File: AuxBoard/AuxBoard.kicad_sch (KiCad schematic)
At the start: 29 parts, among them J1 ATX-24, J10 MatBIn, J11 FanHeader, J2 RPI4B, J4 MatrixASupply, J5 MatrixBSupply, J6 BigLED, J7 MatAOut, J8 MatAIn, J9 MatBOut, Q1 DMMT5401, Q2 DMG2305UX, Q3 DMG2305UX, Q4 DMG2305UX, SW1 SW_DPST, U1 74AHC04

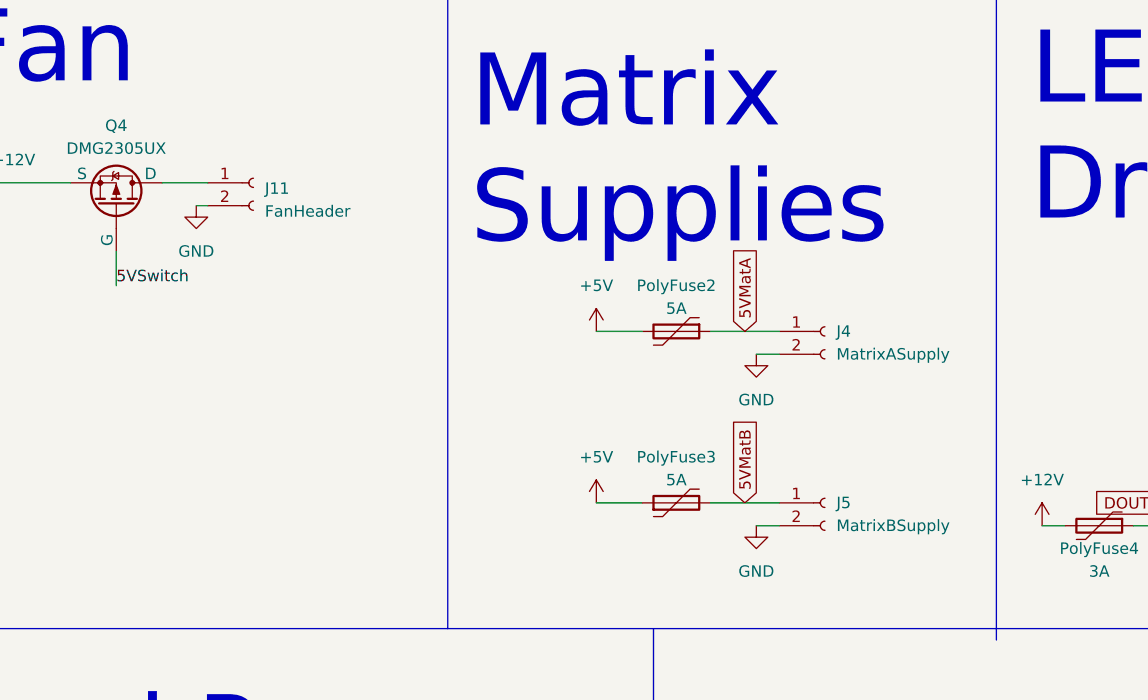
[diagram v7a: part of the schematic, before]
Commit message: Fixing Header Orientation
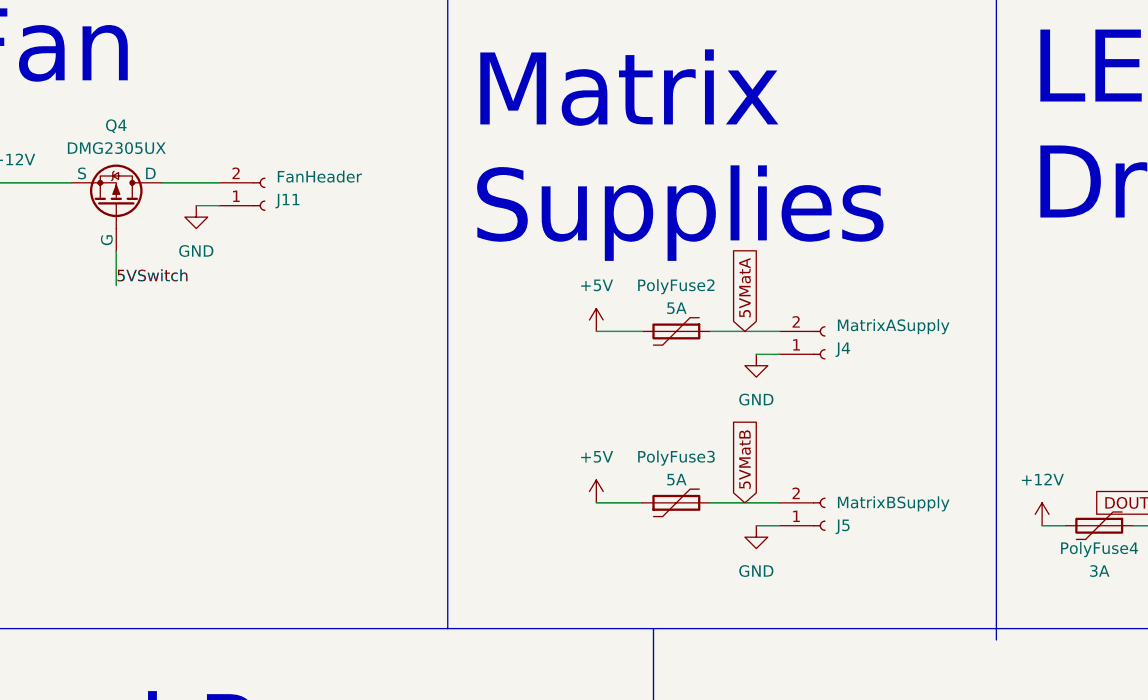
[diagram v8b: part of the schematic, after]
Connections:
- net 5VMatA: now also J4.2 (Pin_2); no longer J4.1 (Pin_1)
- net 5VMatB: now also J5.2 (Pin_2); no longer J5.1 (Pin_1)
- net GND: now also J11.1 (Pin_1), J4.1 (Pin_1), J5.1 (Pin_1); no longer J11.2 (Pin_2), J4.2 (Pin_2), J5.2 (Pin_2)
- net at Q4.1 (D): now also J11.2 (Pin_2); no longer J11.1 (Pin_1)
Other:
- moved on the sheet: J11
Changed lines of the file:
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@@
     (stroke (width 0) (type default))
   )
-  (wire (pts (xy 121.92 34.29) (xy 127 34.29))
+  (wire (pts (xy 190.5 69.85) (xy 182.88 69.85))
     (stroke (width 0) (type default))
   )
@@
     (stroke (width 0) (type default))
   )
+  (wire (pts (xy 121.92 34.29) (xy 128.27 34.29))
+    (stroke (width 0) (type default))
+  )
   (wire (pts (xy 140.97 109.22) (xy 135.89 109.22))
     (stroke (width 0) (type default))
@@
     (stroke (width 0) (type default))
   )
-  (wire (pts (xy 182.88 69.85) (xy 190.5 69.85))
-    (stroke (width 0) (type default))
-  )
   (wire (pts (xy 262.89 67.31) (xy 266.7 67.31))
     (stroke (width 0) (type default))
@@
     (stroke (width 0) (type default))
   )
-  (wire (pts (xy 125.73 36.83) (xy 127 36.83))
-    (stroke (width 0) (type default))
-  )
   (wire (pts (xy 34.29 139.7) (xy 39.37 139.7))
     (stroke (width 0) (type default))
@@
   )
   (wire (pts (xy 91.44 149.86) (xy 96.52 149.86))
+    (stroke (width 0) (type default))
+  )
+  (wire (pts (xy 125.73 36.83) (xy 128.27 36.83))
     (stroke (width 0) (type default))
   )
@@
     )
   )
-  (symbol (lib_id "Connector:Conn_01x02_Female") (at 195.58 69.85 0) (unit 1)
-    (in_bom yes) (on_board yes) (dnp no) (fields_autoplaced)
-    (property "Reference" "J5" (at 196.85 69.8499 0)
-      (effects (font (size 1.27 1.27)) (justify left))
-    )
-    (property "Value" "MatrixBSupply" (at 196.85 72.3899 0)
-      (effects (font (size 1.27 1.27)) (justify left))
-    )
-    (property "Footprint" "Connector_PinSocket_2.54mm:PinSocket_1x02_P2.54mm_Vertical" (at 195.58 69.85 0)
-      (effects (font (size 1.27 1.27)) hide)
-    )
-    (property "Datasheet" "~" (at 195.58 69.85 0)
+  (symbol (lib_id "Connector:Conn_01x02_Female") (at 195.58 72.39 0) (mirror x) (unit 1)
+    (in_bom yes) (on_board yes) (dnp no)
+    (property "Reference" "J5" (at 196.85 72.3901 0)
+      (effects (font (size 1.27 1.27)) (justify left))
+    )
+    (property "Value" "MatrixBSupply" (at 196.85 69.8501 0)
+      (effects (font (size 1.27 1.27)) (justify left))
+    )
+    (property "Footprint" "Connector_PinSocket_2.54mm:PinSocket_1x02_P2.54mm_Vertical" (at 195.58 72.39 0)
+      (effects (font (size 1.27 1.27)) hide)
+    )
+    (property "Datasheet" "~" (at 195.58 72.39 0)
       (effects (font (size 1.27 1.27)) hide)
     )
@@
     )
   )
-  (symbol (lib_id "Connector:Conn_01x02_Female") (at 195.58 50.8 0) (unit 1)
-    (in_bom yes) (on_board yes) (dnp no) (fields_autoplaced)
-    (property "Reference" "J4" (at 196.85 50.7999 0)
-      (effects (font (size 1.27 1.27)) (justify left))
-    )
-    (property "Value" "MatrixASupply" (at 196.85 53.3399 0)
-      (effects (font (size 1.27 1.27)) (justify left))
-    )
-    (property "Footprint" "Connector_PinSocket_2.54mm:PinSocket_1x02_P2.54mm_Vertical" (at 195.58 50.8 0)
-      (effects (font (size 1.27 1.27)) hide)
-    )
-    (property "Datasheet" "~" (at 195.58 50.8 0)
+  (symbol (lib_id "Connector:Conn_01x02_Female") (at 195.58 53.34 0) (mirror x) (unit 1)
+    (in_bom yes) (on_board yes) (dnp no)
+    (property "Reference" "J4" (at 196.85 52.705 0)
+      (effects (font (size 1.27 1.27)) (justify left))
+    )
+    (property "Value" "MatrixASupply" (at 196.85 50.165 0)
+      (effects (font (size 1.27 1.27)) (justify left))
+    )
+    (property "Footprint" "Connector_PinSocket_2.54mm:PinSocket_1x02_P2.54mm_Vertical" (at 195.58 53.34 0)
+      (effects (font (size 1.27 1.27)) hide)
+    )
+    (property "Datasheet" "~" (at 195.58 53.34 0)
       (effects (font (size 1.27 1.27)) hide)
     )
@@
     )
   )
-  (symbol (lib_id "Connector:Conn_01x02_Female") (at 132.08 34.29 0) (unit 1)
-    (in_bom yes) (on_board yes) (dnp no) (fields_autoplaced)
-    (property "Reference" "J11" (at 133.35 34.925 0)
-      (effects (font (size 1.27 1.27)) (justify left))
-    )
-    (property "Value" "FanHeader" (at 133.35 37.465 0)
-      (effects (font (size 1.27 1.27)) (justify left))
-    )
-    (property "Footprint" "Connector_PinSocket_2.54mm:PinSocket_1x02_P2.54mm_Vertical" (at 132.08 34.29 0)
-      (effects (font (size 1.27 1.27)) hide)
-    )
-    (property "Datasheet" "~" (at 132.08 34.29 0)
-      (effects (font (size 1.27 1.27)) hide)
-    )
+  (symbol (lib_id "Connector:Conn_01x02_Female") (at 133.35 36.83 0) (mirror x) (unit 1)
+    (in_bom yes) (on_board yes) (dnp no)
+    (property "Reference" "J11" (at 134.62 36.195 0)
+      (effects (font (size 1.27 1.27)) (justify left))
+    )
+    (property "Value" "FanHeader" (at 134.62 33.655 0)
+      (effects (font (size 1.27 1.27)) (justify left))
+    )
+    (property "Footprint" "Connector_PinSocket_2.54mm:PinSocket_1x02_P2.54mm_Vertical" (at 133.35 36.83 0)
+      (effects (font (size 1.27 1.27)) hide)
+    )
+    (property "Datasheet" "~" (at 133.35 36.83 0)
+      (effects (font (size 1.27 1.27)) hide)
+    )
